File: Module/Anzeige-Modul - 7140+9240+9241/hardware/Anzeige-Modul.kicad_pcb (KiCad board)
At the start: 2 copper layers, 137 x 102 mm, 61 parts, among them J10 gn, J11 or, J12 rt, J13 br, J2 vi, J3 Conn_02x03_Counter_Clockwise, J4 rs, J5 Conn_01x13_Male, J6 Conn_01x16_Male, J7 gr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

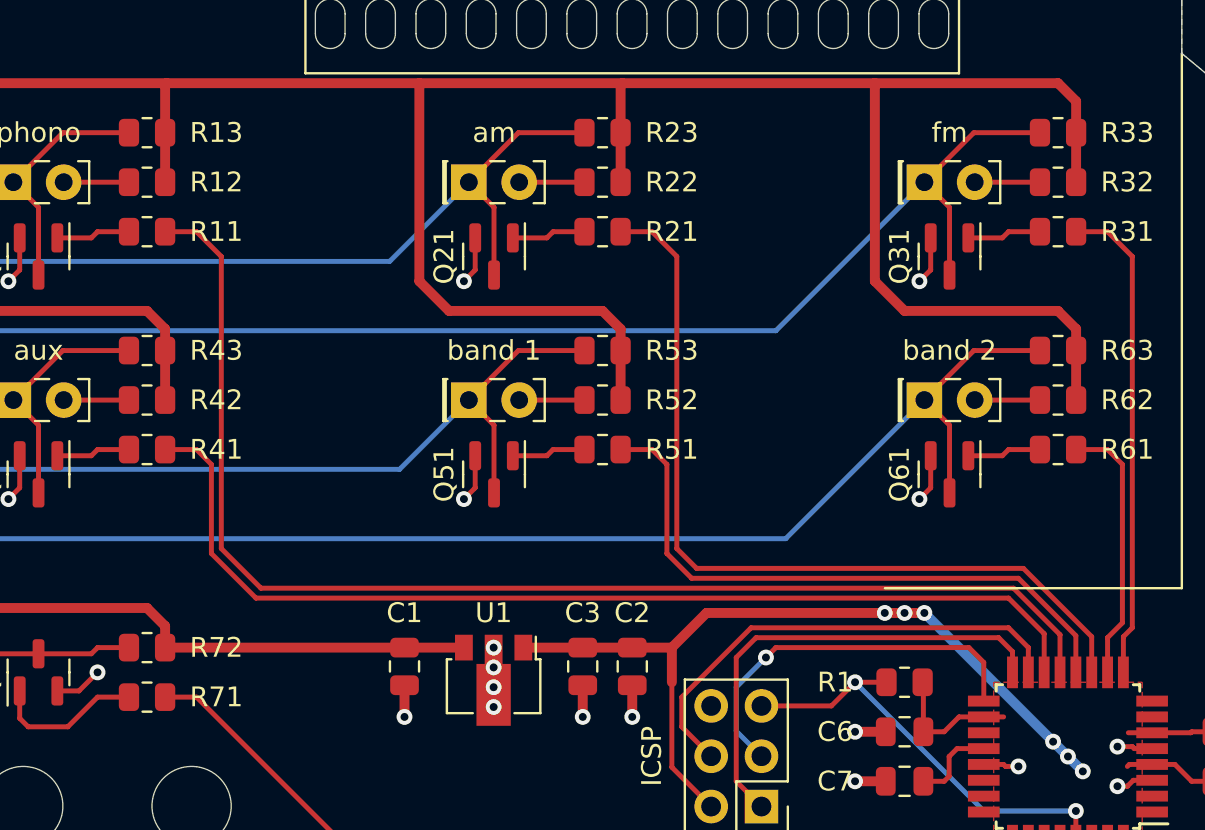
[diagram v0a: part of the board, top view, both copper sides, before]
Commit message: Stereo-Decoder 4-Spulen / Anzeige-Modul überarbeitet
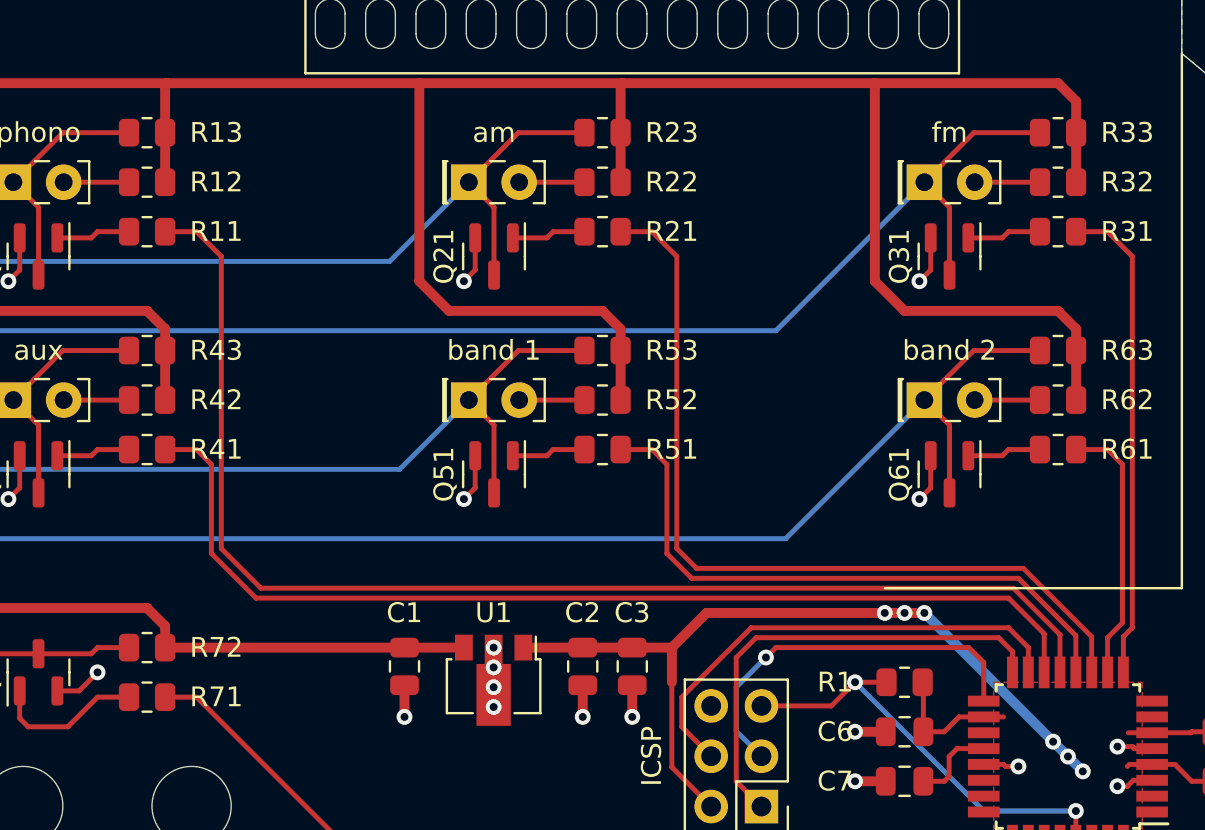
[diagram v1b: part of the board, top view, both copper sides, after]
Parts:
- C1: value 330nF -> 470n
- C2: renamed from C3; value 2.2µF -> 2.2µ
- C3: renamed from C2; value 100nF -> 100n
- C4, C5, C6, C7: value 100nF -> 100n
